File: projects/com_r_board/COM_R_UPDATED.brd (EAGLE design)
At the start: 90.2 x 95.9 mm, 19 parts, among them J1 0532610471, J2 53398-1271, J3 504050-0691, J4 ESQ-126-39-G-D, J5 ESQ-126-39-G-D, J6 G125-MS10605L3P, J7 61300411121

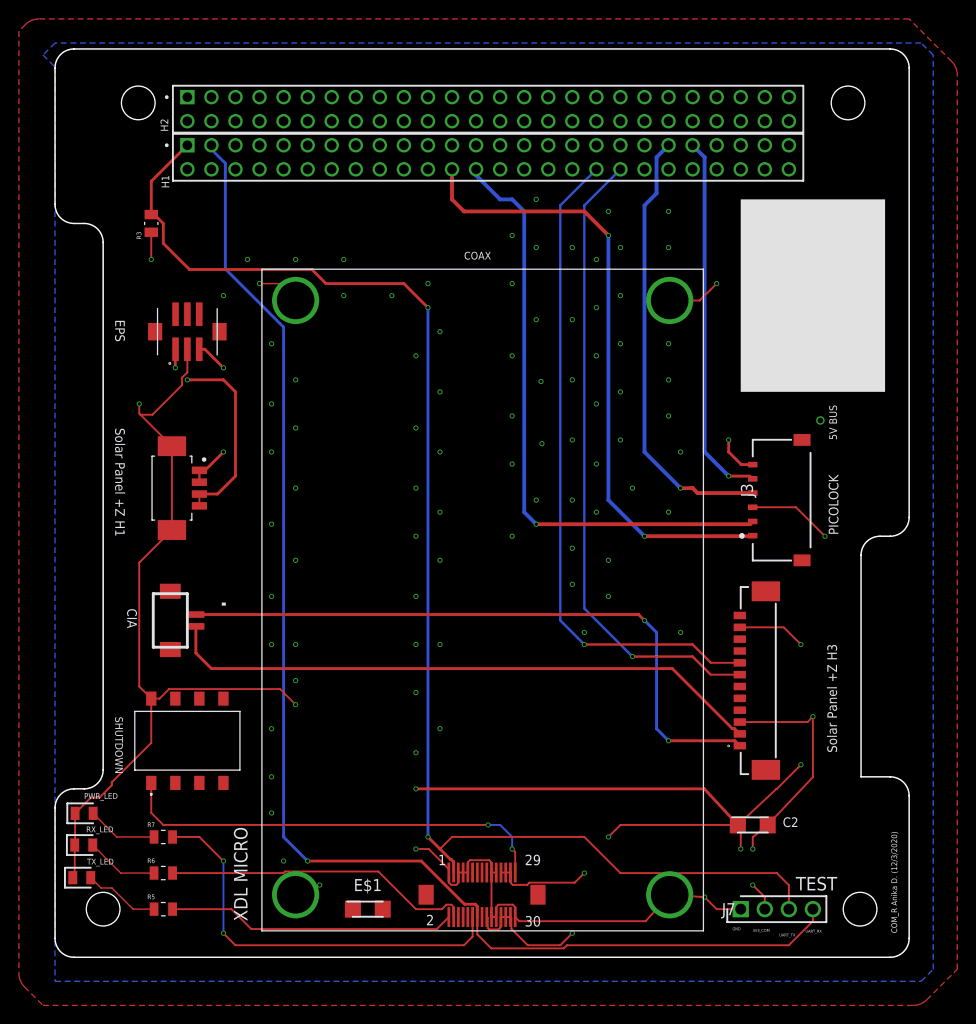
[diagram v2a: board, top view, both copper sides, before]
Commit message: Fixed PC104 mounting holes and updated pc104 pinouts to be updated
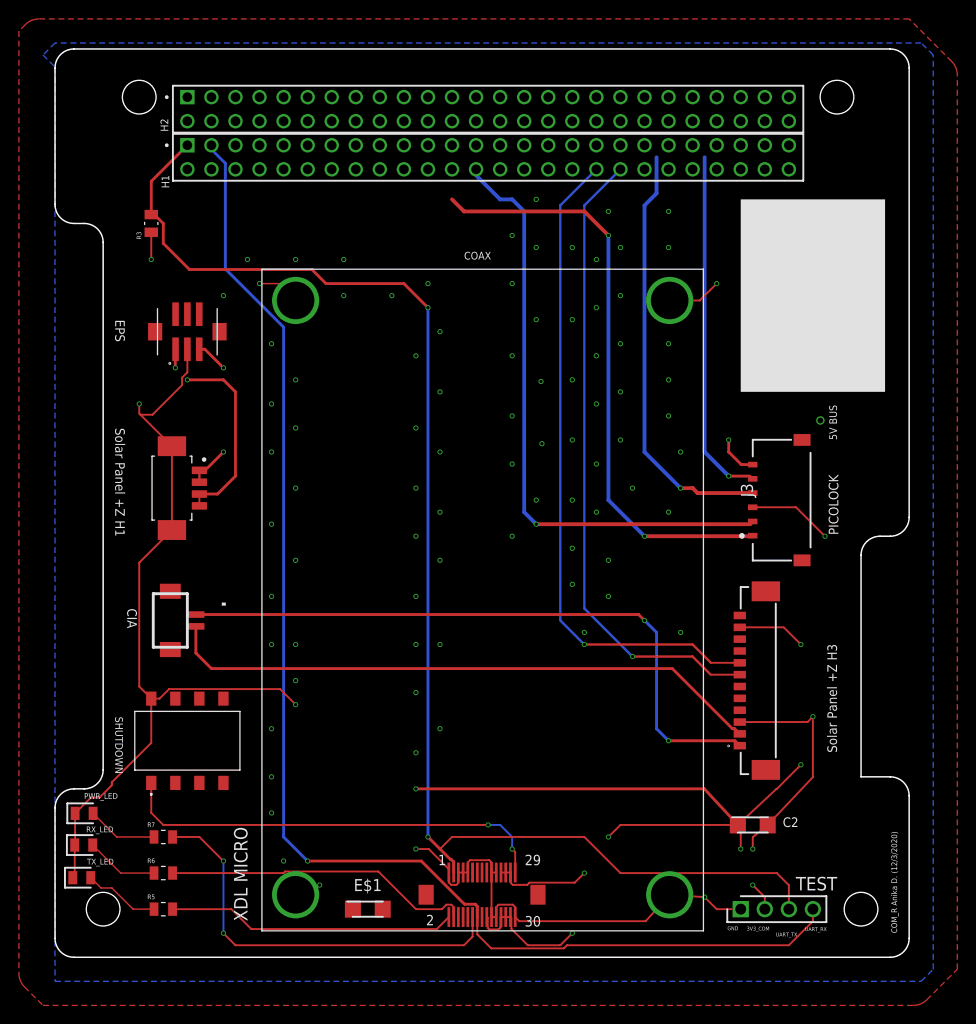
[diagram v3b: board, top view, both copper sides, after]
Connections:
- net ANT_BURN1: now also J4.23; no longer J4.24
- net ANT_BURN2: now also J4.25; no longer J4.26
- net I2C_SCL: now also J4.44; no longer J4.43
- net I2C_SDA: now also J4.42; no longer J4.41
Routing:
- net ANT_BURN1: track 66.0 -> 62.9 mm
- net I2C_SDA: track 46.7 -> 44.9 mm
- net I2C_SCL: track 39.2 -> 37.4 mm
- net ANT_BURN2: track 63.8 -> 63.2 mm
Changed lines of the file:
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@@
 <setting verticaltext="up"/>
 </settings>
-<grid distance="50" unitdist="mil" unit="mm" style="lines" multiple="1" display="no" altdistance="0.000003125" altunitdist="mm" altunit="mm"/>
+<grid distance="50" unitdist="mil" unit="inch" style="lines" multiple="1" display="no" altdistance="0.000000123031" altunitdist="inch" altunit="inch"/>
 <layers>
 <layer number="1" name="Top" color="4" fill="1" visible="yes" active="yes"/>
@@
 <text x="11.9576875" y="87.158325" size="0.8128" layer="21" rot="R90">H2</text>
 <text x="12.063225" y="81.1811" size="0.8128" layer="21" rot="R90">H1</text>
-<hole x="83.7184" y="90.1954" drill="3.556"/>
+<hole x="82.55" y="90.805" drill="3.556"/>
 <wire x1="0" y1="15.78" x2="0" y2="2" width="0.1524" layer="20"/>
 <wire x1="0" y1="2" x2="2" y2="0" width="0.1524" layer="20" curve="90"/>
@@
 <wire x1="3.08" y1="17.78" x2="2" y2="17.78" width="0.1524" layer="20"/>
 <wire x1="2" y1="17.78" x2="0" y2="15.78" width="0.1524" layer="20" curve="90"/>
-<hole x="8.7884" y="90.1954" drill="3.556"/>
+<hole x="8.89" y="90.805" drill="3.556"/>
 <hole x="5.08" y="5.08" drill="3.556"/>
-<hole x="84.9884" y="5.08" drill="3.556"/>
+<hole x="85.09" y="5.08" drill="3.556"/>
 <text x="7.62" y="36.83" size="1.016" layer="21" rot="SR270">CIA</text>
 <text x="82.55" y="21.59" size="1.016" layer="21" rot="R90">Solar Panel +Z H3</text>
@@
 <text x="76.82310625" y="13.7543875" size="1.016" layer="21">C2</text>
 <text x="82.55" y="54.61" size="0.8128" layer="21" rot="SR90">5V BUS</text>
-<text x="71.518459375" y="2.852059375" size="0.3048" layer="21">GND</text>
-<text x="73.641215625" y="2.684690625" size="0.3048" layer="21">3V3_COM</text>
-<text x="76.456896875" y="2.201578125" size="0.3048" layer="21">UART_TX
+<text x="70.982428125" y="2.852059375" size="0.4064" layer="21">GND</text>
+<text x="73.020546875" y="2.825765625" size="0.4064" layer="21">3V3_COM</text>
+<text x="76.0901375" y="2.201578125" size="0.4064" layer="21">UART_TX
 </text>
-<text x="79.22145625" y="2.596403125" size="0.3048" layer="21">UART_RX</text>
+<text x="79.165034375" y="2.765684375" size="0.4064" layer="21">UART_RX</text>
 <text x="88.9" y="2.54" size="0.6096" layer="21" rot="R90">COM_R Anika D. (12/3/2020)</text>
 </plain>
@@
 <attribute name="MOUSER_PART_NUMBER" value="710-61300411121" x="72.39" y="5.08" size="1.778" layer="27" display="off"/>
 <attribute name="MOUSER_PRICE-STOCK" value="https://www.mouser.co.uk/ProductDetail/Wurth-Elektronik/61300411121?qs=PhR8RmCirEYQcLLqXD8rAA%3D%3D" x="72.39" y="5.08" size="1.778" layer="27" display="off"/>
-<attribute name="NAME" x="71.12" y="5.08" size="1.27" layer="25" align="center"/>
 </element>
 <element name="R3" library="TNPW080510K0BETY" package="RESC2012X55N" value="TNPW080510K0BETY" x="10.16" y="77.47" smashed="yes" rot="R90">
@@
 </signal>
 <signal name="ANT_BURN1">
-<contactref element="J4" pad="24"/>
 <contactref element="J3" pad="1"/>
 <via x="62.23" y="44.45" extent="1-16" drill="0.35"/>
 <wire x1="62.23" y1="44.45" x2="58.42" y2="48.26" width="0.4064" layer="16"/>
 <wire x1="41.91" y1="80.01" x2="43.18" y2="78.74" width="0.4064" layer="1"/>
-<wire x1="41.91" y1="80.01" x2="41.91" y2="83.185" width="0.4064" layer="1"/>
 <wire x1="55.88" y1="78.74" x2="43.18" y2="78.74" width="0.4064" layer="1"/>
 <wire x1="58.42" y1="76.2" x2="58.42" y2="48.26" width="0.4064" layer="16"/>
@@
 <wire x1="62.23" y1="44.45" x2="73.6" y2="44.45" width="0.4064" layer="1"/>
 <wire x1="73.6" y1="44.45" x2="73.66" y2="44.51" width="0.4064" layer="1"/>
+<contactref element="J4" pad="23"/>
+<wire x1="41.91" y1="80.01" x2="41.91" y2="85.725" width="0" layer="19" extent="1-1"/>
 </signal>
 <signal name="ANT_BURN2">
-<contactref element="J4" pad="26"/>
 <contactref element="J3" pad="2"/>
 <wire x1="44.45" y1="82.55" x2="46.99" y2="80.01" width="0.4064" layer="16"/>
-<wire x1="44.45" y1="82.55" x2="44.45" y2="83.185" width="0.4064" layer="16"/>
 <wire x1="73.66" y1="46.01" x2="73.37" y2="45.72" width="0.4064" layer="1"/>
 <wire x1="46.99" y1="80.01" x2="48.26" y2="80.01" width="0.4064" layer="16"/>
@@
 <via x="50.8" y="45.72" extent="1-16" drill="0.35"/>
 <wire x1="73.37" y1="45.72" x2="50.8" y2="45.72" width="0.4064" layer="1"/>
+<contactref element="J4" pad="25"/>
+<wire x1="44.45" y1="82.55" x2="44.45" y2="85.725" width="0" layer="19" extent="16-16"/>
 </signal>
 <signal name="SA_RTN">
@@
 <signal name="I2C_SDA">
 <contactref element="J3" pad="4"/>
-<contactref element="J4" pad="41"/>
 <via x="66.04" y="49.53" extent="1-16" drill="0.35"/>
 <wire x1="62.23" y1="79.375" x2="62.23" y2="53.34" width="0.4064" layer="16"/>
 <wire x1="66.04" y1="49.53" x2="62.23" y2="53.34" width="0.4064" layer="16"/>
 <wire x1="63.5" y1="80.645" x2="62.23" y2="79.375" width="0.4064" layer="16"/>
-<wire x1="63.5" y1="84.455" x2="64.77" y2="85.725" width="0.4064" layer="16"/>
 <wire x1="63.5" y1="84.455" x2="63.5" y2="80.645" width="0.4064" layer="16"/>
 <wire x1="66.04" y1="49.53" x2="67.31" y2="49.53" width="0.4064" layer="1"/>
 <wire x1="67.83" y1="49.01" x2="73.66" y2="49.01" width="0.4064" layer="1"/>
 <wire x1="67.31" y1="49.53" x2="67.83" y2="49.01" width="0.4064" layer="1"/>
+<contactref element="J4" pad="42"/>
+<wire x1="63.5" y1="84.455" x2="64.77" y2="83.185" width="0" layer="19" extent="16-16"/>
 </signal>
 <signal name="I2C_SCL">
 <contactref element="J3" pad="5"/>
-<contactref element="J4" pad="43"/>
 <via x="71.12" y="50.8" extent="1-16" drill="0.35"/>
 <wire x1="71.12" y1="50.8" x2="68.58" y2="53.34" width="0.4064" layer="16"/>
-<wire x1="67.31" y1="85.725" x2="68.58" y2="84.455" width="0.4064" layer="16"/>
 <wire x1="68.58" y1="84.455" x2="68.58" y2="53.34" width="0.4064" layer="16"/>
 <wire x1="73.66" y1="50.51" x2="73.37" y2="50.8" width="0.2032" layer="1"/>
 <wire x1="73.37" y1="50.8" x2="71.12" y2="50.8" width="0.3048" layer="1"/>
+<contactref element="J4" pad="44"/>
+<wire x1="68.58" y1="84.455" x2="67.31" y2="83.185" width="0" layer="19" extent="16-16"/>
 </signal>
 <signal name="SHUTDOWN">
